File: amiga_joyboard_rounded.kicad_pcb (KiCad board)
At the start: 2 copper layers, 192.5 x 63.5 mm, 27 parts, among them J1 JOYPORT_OUT, J2 CONN_D, J3 CONN_F, SW1 FIRE_BTN, SW2 B_BTN, SW3 A_BTN, SW4 RIGHT_BTN, SW5 LEFT_BTN, SW6 DOWN_BTN, SW7 UP_BTN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

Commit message: cosmetics, logos
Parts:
- added REF**: OSHW-Symbol_8.9x8mm_Copper, Symbol:OSHW-Symbol_8.9x8mm_Copper, B.Cu at (217.9, 77.2)
- added REF**: OSHW-Symbol_8.9x8mm_Copper, Symbol:OSHW-Symbol_8.9x8mm_Copper, B.Cu at (65.0, 92.5)

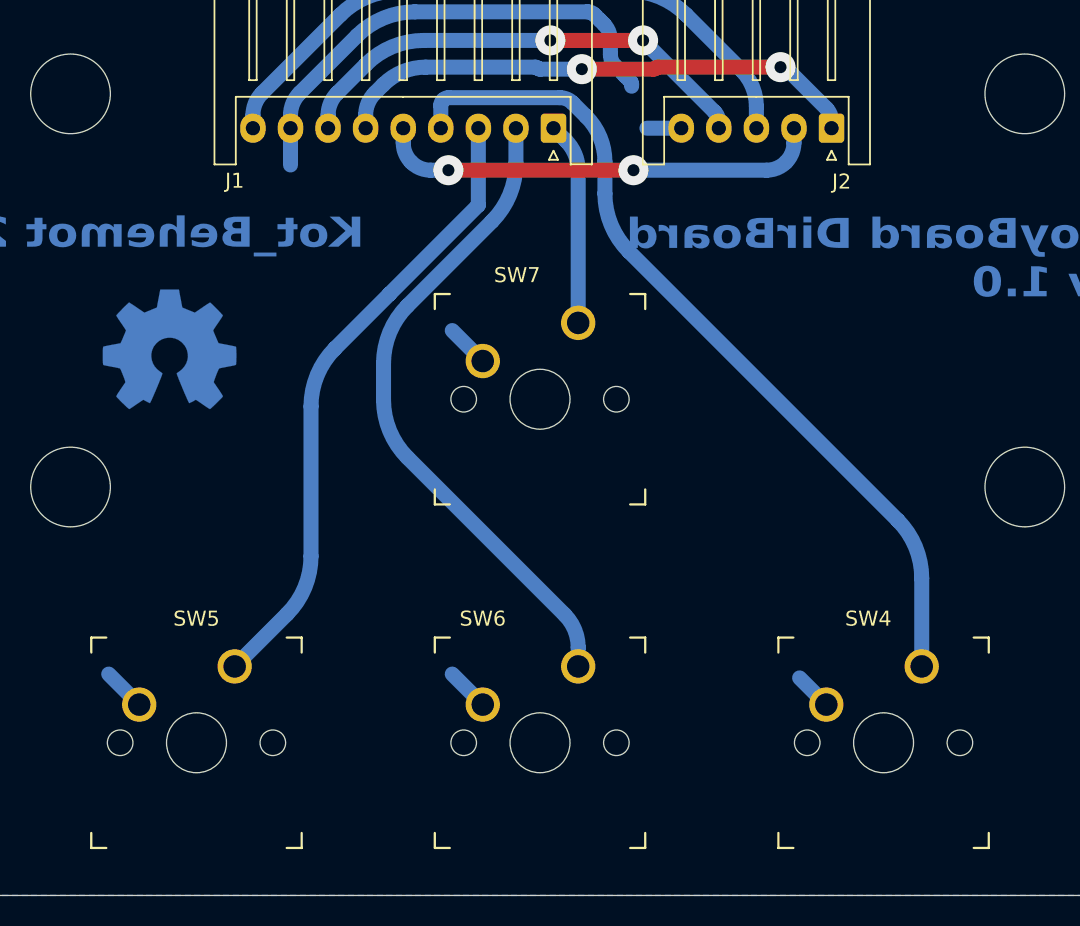
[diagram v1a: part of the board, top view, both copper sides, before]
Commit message: dir buttons moved closer together
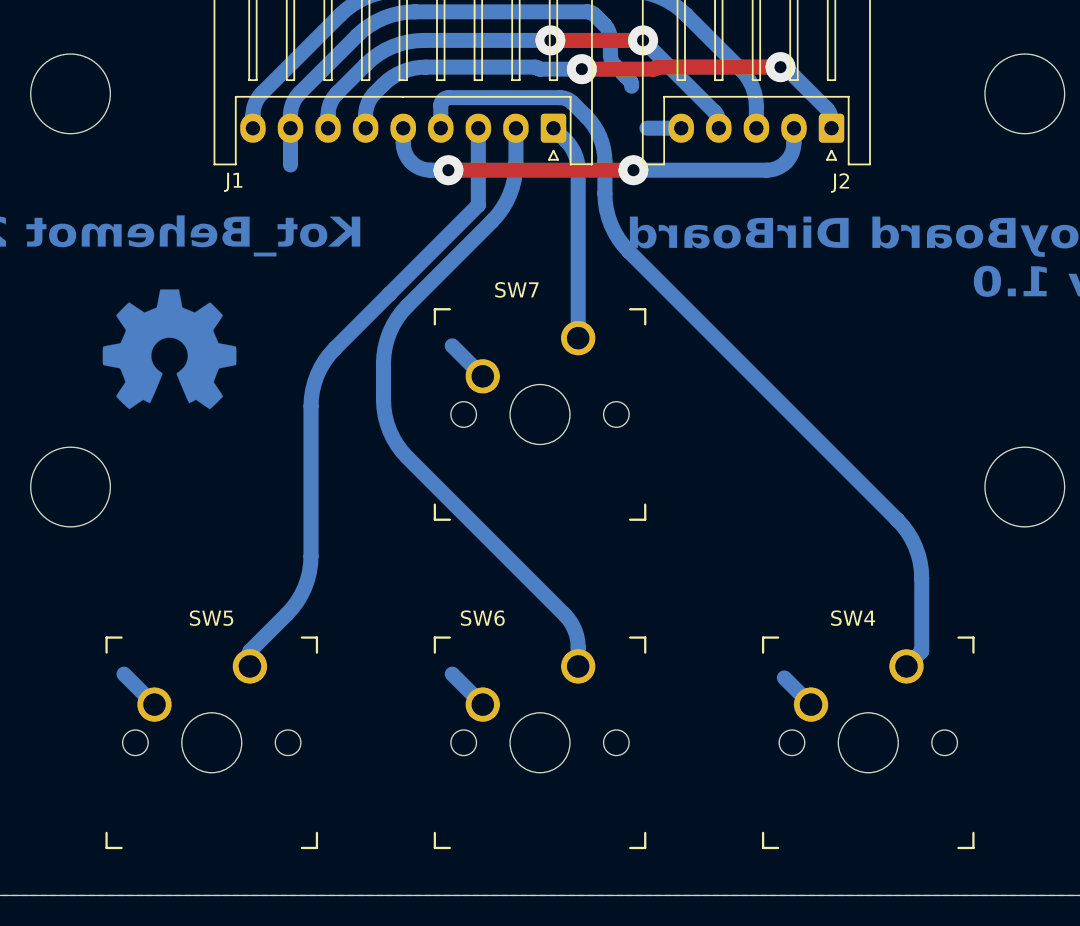
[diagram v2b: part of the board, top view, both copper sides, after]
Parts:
- moved SW4 1.02 mm to (111.5, 118.6)
- moved SW7 1.02 mm to (89.7, 96.8)
- moved SW5 1.02 mm to (67.8, 118.6)
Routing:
- net /UP: track 13.5 -> 14.5 mm

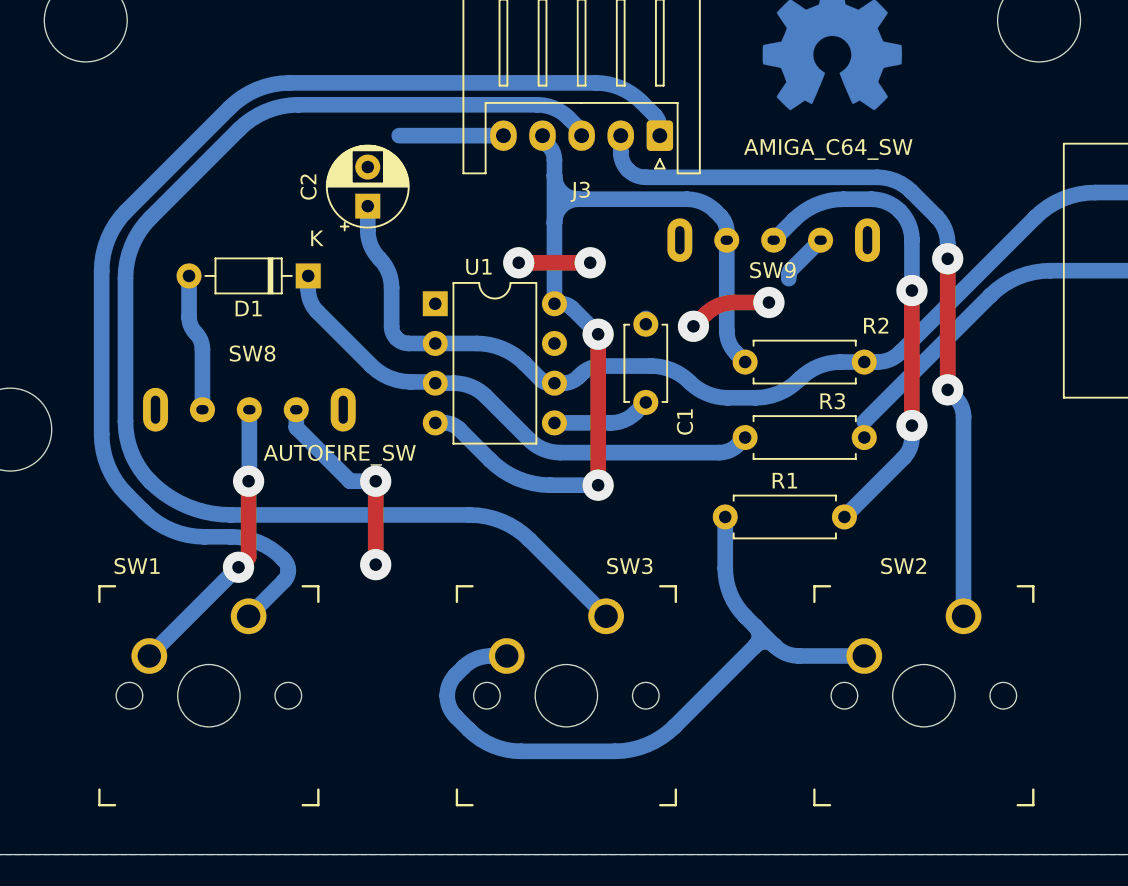
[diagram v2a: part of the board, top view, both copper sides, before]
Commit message: more button movement
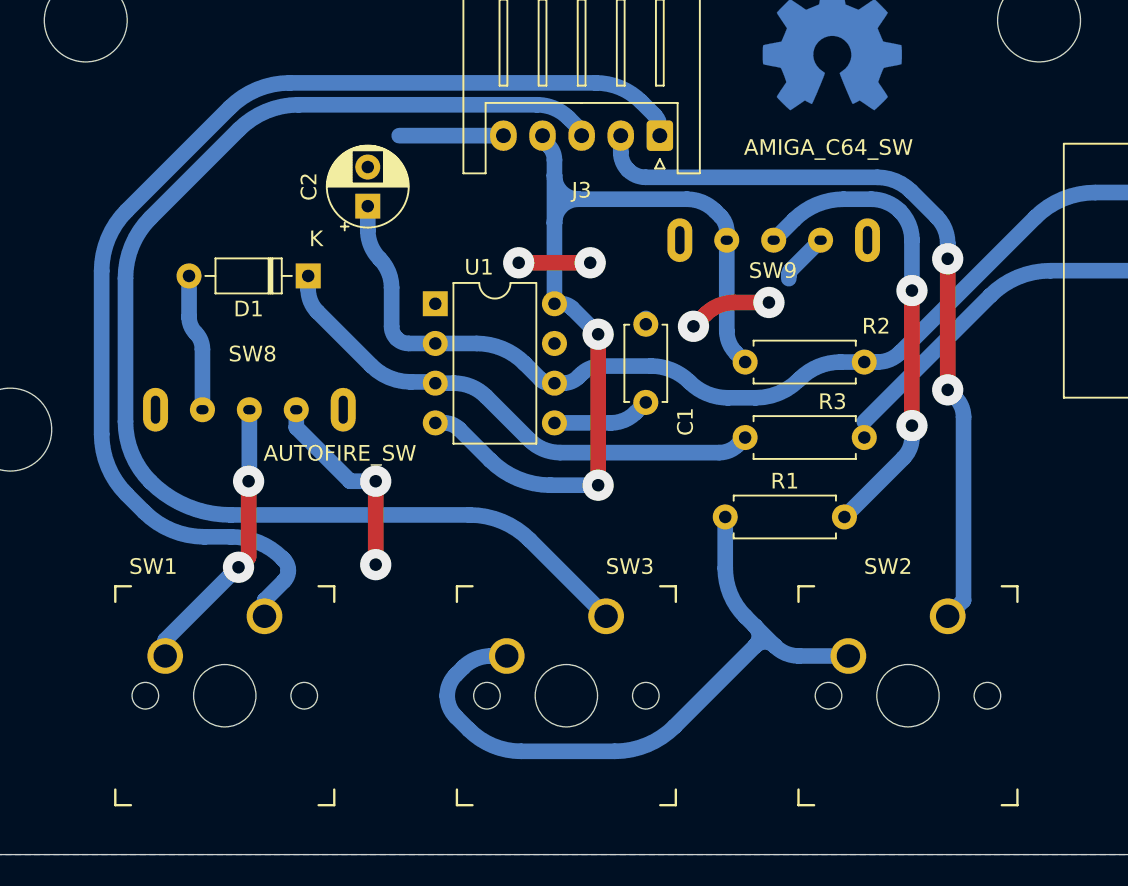
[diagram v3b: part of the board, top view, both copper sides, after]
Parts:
- moved SW1 1.02 mm to (179.1, 118.6)
- moved SW2 1.02 mm to (222.8, 118.6)
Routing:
- net Net-(R1-Pad1): track 46.9 -> 45.9 mm
